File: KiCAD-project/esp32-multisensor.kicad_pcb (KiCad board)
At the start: 2 copper layers, 50 x 50 mm, 12 parts, among them J1 USB_C_Receptacle_USB2.0, SW1 RST, SW3 BOOT, U1 ESP32-WROOM-E, U2 AMS1117-3.3, U3 TPD4E02B04DQA

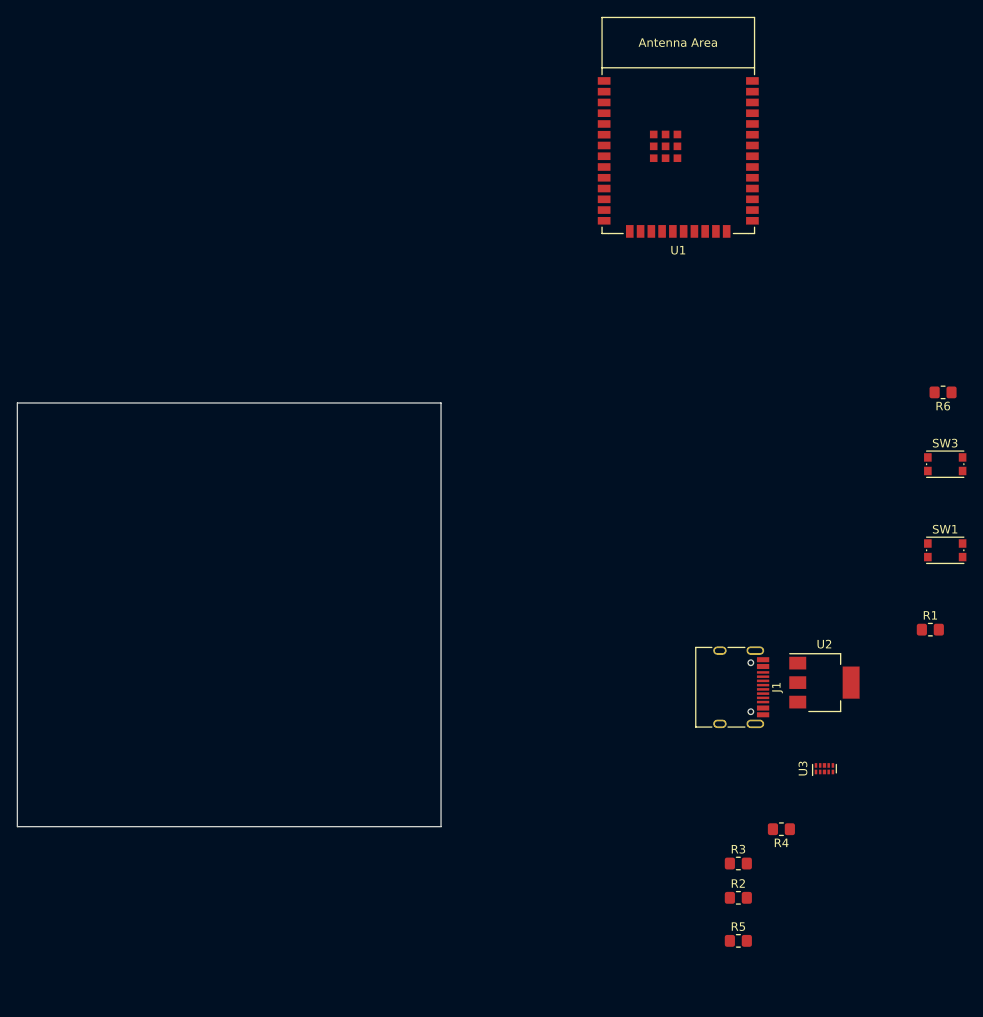
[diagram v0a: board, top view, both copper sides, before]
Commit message: schematic created + base pcb
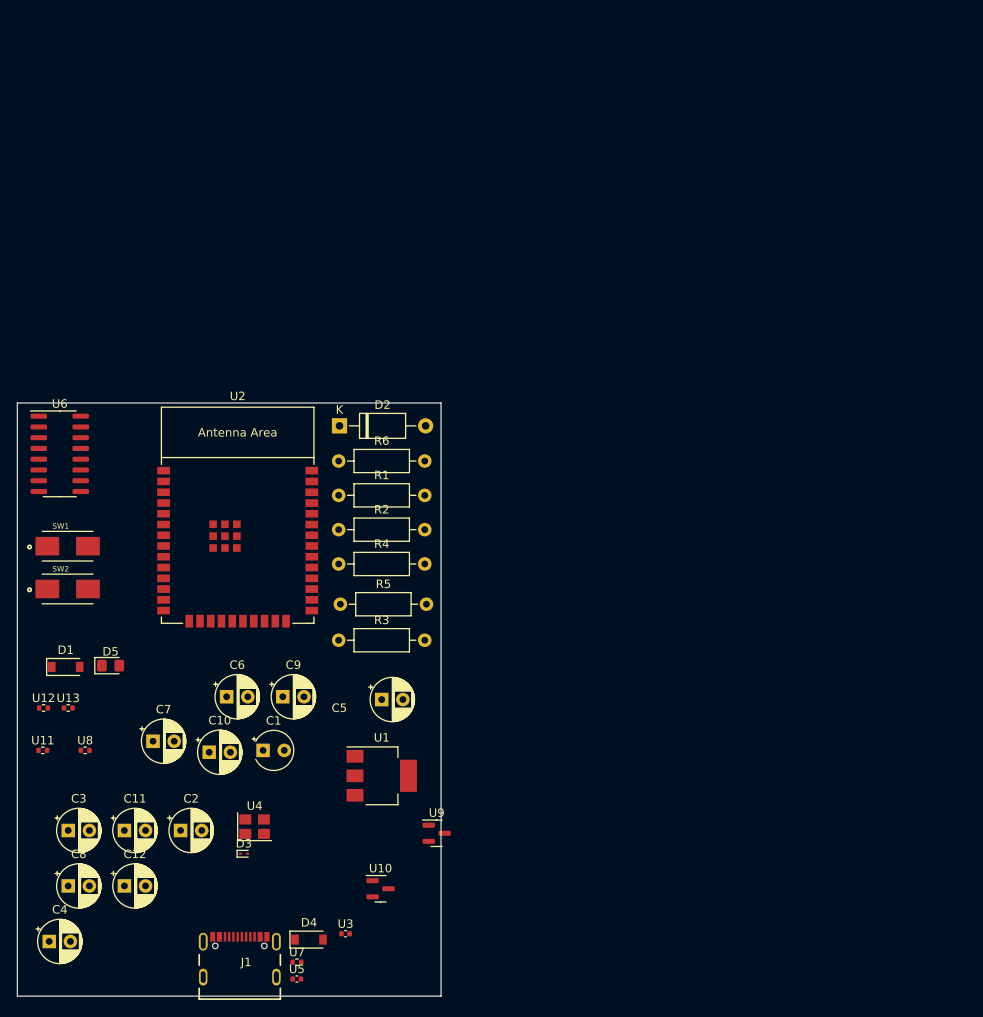
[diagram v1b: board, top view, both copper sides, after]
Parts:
- removed SW3: BOOT, Button_Switch_SMD:SW_Push_1P1T_NO_CK_KMR2
- added C1: 10uF, Capacitor_THT:CP_Radial_Tantal_D4.5mm_P2.50mm, F.Cu at (169.0, 114.0)
- added C10: 10nF 10V, Capacitor_THT:CP_Radial_D5.0mm_P2.50mm, F.Cu at (162.6, 114.2)
- added C11: 100nF, Capacitor_THT:CP_Radial_D5.0mm_P2.50mm, F.Cu at (152.6, 123.5)
- added C12: 100nF, Capacitor_THT:CP_Radial_D5.0mm_P2.50mm, F.Cu at (152.6, 130.0)
- added C2: 100nF, Capacitor_THT:CP_Radial_D5.0mm_P2.50mm, F.Cu at (159.3, 123.5)
- added C3: 100nF, Capacitor_THT:CP_Radial_D5.0mm_P2.50mm, F.Cu at (146.0, 123.5)
- added C4: 22uF, Capacitor_THT:CP_Radial_D5.0mm_P2.50mm, F.Cu at (143.8, 136.6)
- added C5: 22pF, Capacitor_THT:CP_Radial_D5.0mm_P2.50mm, F.Cu at (183.0, 108.0)
- added C6: 22pF, Capacitor_THT:CP_Radial_D5.0mm_P2.50mm, F.Cu at (164.7, 107.7)
- added C7: 1uF 16V, Capacitor_THT:CP_Radial_D5.0mm_P2.50mm, F.Cu at (156.0, 112.9)
- added C8: 1uF 16V, Capacitor_THT:CP_Radial_D5.0mm_P2.50mm, F.Cu at (146.0, 130.0)
- added C9: 100nF 10V, Capacitor_THT:CP_Radial_D5.0mm_P2.50mm, F.Cu at (171.3, 107.7)
- added D1: LESD5D5.0CT1G, Diode_SMD:D_SOD-123, F.Cu at (145.7, 104.2)
- added D2: B5819W, Diode_THT:D_A-405_P10.16mm_Horizontal, F.Cu at (178.0, 75.7)
- added D3: LESD5D5.0CT1G, Diode_SMD:D_SOD-923, F.Cu at (166.7, 126.2)
- added D4: LESD5D5.0CT1G, Diode_SMD:D_SOD-123, F.Cu at (174.4, 136.3)
- added D5: LED, LED_SMD:LED_0805_2012Metric_Pad1.15x1.40mm_HandSolder, F.Cu at (151.0, 104.0)
- added SW2: SW_Push, esp32_multisensor:SW_147873-2, F.Cu at (145.9, 95.0)
- added U10: SS8050, Package_TO_SOT_SMD:SOT-23, F.Cu at (182.9, 130.3)
- added U11: 330 R, Resistor_SMD:R_0402_1005Metric, F.Cu at (143.0, 114.0)
- added U12: 330 R, Resistor_SMD:R_0402_1005Metric, F.Cu at (143.1, 109.0)
- added U13: 330 R, Resistor_SMD:R_0402_1005Metric, F.Cu at (146.0, 109.0)
- added U4: 12MHz, Crystal:Crystal_SMD_3225-4Pin_3.2x2.5mm, F.Cu at (168.0, 123.0)
- added U5: 22 pF, Capacitor_SMD:C_0402_1005Metric, F.Cu at (173.0, 141.0)
- added U6: CH340G, Package_SO:SOIC-16_3.9x9.9mm_P1.27mm, F.Cu at (145.0, 79.0)
- added U7: 5.1kR, Resistor_SMD:R_0402_1005Metric, F.Cu at (173.0, 139.0)
- added U8: 5.1kR, Resistor_SMD:R_0402_1005Metric, F.Cu at (148.0, 114.0)
- added U9: SS8050, Package_TO_SOT_SMD:SOT-23, F.Cu at (189.5, 123.8)
- J1: value USB_C_Receptacle_USB2.0 -> USB4105-GF-A; footprint Connector_USB:USB_C_Receptacle_HRO_TYPE-C-31-M-12 -> esp32_multisensor:GCT_USB4105-GF-A
- R1: value 10k -> 0R 1%; footprint Resistor_SMD:R_0805_2012Metric_Pad1.20x1.40mm_HandSolder -> Resistor_THT:R_Axial_DIN0207_L6.3mm_D2.5mm_P10.16mm_Horizontal
- R2: value 1M -> 5k1R 1%; footprint Resistor_SMD:R_0805_2012Metric_Pad1.20x1.40mm_HandSolder -> Resistor_THT:R_Axial_DIN0207_L6.3mm_D2.5mm_P10.16mm_Horizontal
- R3: value 5k1 -> 10kR 1%; footprint Resistor_SMD:R_0805_2012Metric_Pad1.20x1.40mm_HandSolder -> Resistor_THT:R_Axial_DIN0207_L6.3mm_D2.5mm_P10.16mm_Horizontal
- R4: value 5k1 -> 5k1R 1%; footprint Resistor_SMD:R_0805_2012Metric_Pad1.20x1.40mm_HandSolder -> Resistor_THT:R_Axial_DIN0207_L6.3mm_D2.5mm_P10.16mm_Horizontal
- R5: footprint Resistor_SMD:R_0805_2012Metric_Pad1.20x1.40mm_HandSolder -> Resistor_THT:R_Axial_DIN0207_L6.3mm_D2.5mm_P10.16mm_Horizontal
- R6: value 10k -> 10kR 1%; footprint Resistor_SMD:R_0805_2012Metric_Pad1.20x1.40mm_HandSolder -> Resistor_THT:R_Axial_DIN0207_L6.3mm_D2.5mm_P10.16mm_Horizontal
- SW1: value RST -> SW_Push; footprint Button_Switch_SMD:SW_Push_1P1T_NO_CK_KMR2 -> esp32_multisensor:SW_147873-2
- U1: value ESP32-WROOM-E -> AMS1117-3.3; footprint espressif:ESP32-WROOM-32E -> Package_TO_SOT_SMD:SOT-223-3_TabPin2
- U2: value AMS1117-3.3 -> ESP32-WROOM-E; footprint Package_TO_SOT_SMD:SOT-223-3_TabPin2 -> espressif:ESP32-WROOM-32E
- U3: value TPD4E02B04DQA -> 22 pF; footprint Package_SON:USON-10_2.5x1.0mm_P0.5mm -> Capacitor_SMD:C_0402_1005Metric
- moved SW1 103.6 mm to (145.9, 89.9)
- moved U1 82.8 mm to (183.0, 117.0)
- moved R6 71.8 mm to (177.9, 79.8), turned to 0 degrees
- moved R1 71.6 mm to (177.9, 83.9)
- moved U2 71.6 mm to (166.0, 88.0)
- moved J1 67.1 mm to (166.2, 140.8), turned to 0 degrees
- moved R2 64.1 mm to (177.9, 88.0)
- moved R5 61.5 mm to (178.1, 96.8)
- moved R4 60.9 mm to (177.9, 92.0), turned to 0 degrees
- moved U3 59.8 mm to (178.7, 135.6), turned to 0 degrees
- moved R3 54.0 mm to (177.9, 101.0)
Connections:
- J1 pad A5: Net-(R4-Pad1) -> CC1
- J1 pad A6: Data+ -> USB_D+
- J1 pad A7: Data- -> USB_D-
- J1 pad B5: Net-(R3-Pad1) -> CC1
- J1 pad B6: Data+ -> USB_D+
- J1 pad B7: Data- -> USB_D-
- R1 pad 1: Net-(SW1-Pad2) -> Net-(J1-PadS1)
- R1 pad 2: +3V3 -> GND
- R2 pad 1: Net-(J1-PadS1) -> CC1
- R3 pad 1: Net-(R3-Pad1) -> +3V3
- R3 pad 2: GND -> IO9_BOOT
- R4 pad 1: Net-(R4-Pad1) -> CC1
- R6 pad 1: Net-(U1-Pad25) -> +3V3
- R6 pad 2: +3V3 -> CHIP_PU
- SW1 pad 1: GND -> IO9_BOOT
- SW1 pad 2: Net-(SW1-Pad2) -> GND
- U1 pad 3: +3V3 -> +5V
- U2 pad 3: +5V -> CHIP_PU
- U3 pad 1: +5V -> Net-(U3-Pad1)
- U3 pad 2: unconnected-(U3-Pad2) -> GND
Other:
- board size 50 x 50 mm -> 50 x 70 mm
